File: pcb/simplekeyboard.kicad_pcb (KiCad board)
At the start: 2 copper layers, 288.1 x 97.6 mm, 164 parts, among them J1 USB_C_Receptacle_USB2.0_16P, J2 Conn_ARM_JTAG_SWD_10, SW1 SW_Push, SW10 SW_Push, SW11 SW_Push, SW12 SW_Push, SW13 SW_Push, SW14 SW_Push, SW15 SW_Push, SW16 SW_Push, SW17 SW_Push, SW18 SW_Push, SW19 SW_Push, SW2 SW_Push, SW20 SW_Push, SW21 SW_Push, SW22 SW_Push, SW23 SW_Push, SW24 SW_Push, SW25 SW_Push, SW26 SW_Push, SW27 SW_Push, SW28 SW_Push, SW29 SW_Push, SW3 SW_Push, SW30 SW_Push, SW31 SW_Push, SW32 SW_Push, SW33 SW_Push, SW34 SW_Push, SW35 SW_Push, SW36 SW_Push, SW37 SW_Push, SW38 SW_Push, SW39 SW_Push, SW4 SW_Push, SW40 SW_Push, SW41 SW_Push, SW42 SW_Push, SW43 SW_Push, SW44 SW_Push, SW45 SW_Push, SW46 SW_Push, SW47 SW_Push, SW48 SW_Push, SW49 SW_Push, SW5 SW_Push, SW50 SW_Push, SW51 SW_Push, SW52 SW_Push, SW53 SW_Push, SW54 SW_Push, SW55 SW_Push, SW56 SW_Push, SW57 SW_Push, SW58 SW_Push, SW59 SW_Push, SW6 SW_Push, SW60 SW_Push, SW61 SW_Push, SW62 SW_SPDT, SW63 SW_Push, SW7 SW_Push, SW8 SW_Push, SW9 SW_Push, U1 STM32F072CBT6, U2 USBLC6-2SC6, U3 LD39050PU33R, U4 MCP23017_SO, U5 MCP23008-xSO

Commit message: Added version marking
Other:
- board text added: "simplekeyboard v1"
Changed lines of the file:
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@@
 		(layer "Edge.Cuts")
+	)
+	(gr_text "simplekeyboard v1"
+		(at 28.575 123.825 0)
+		(layer "F.SilkS")
+		(effects
+			(font
+				(size 1.5 1.5)
+				(thickness 0.3)
+				(bold yes)
+			)
+			(justify left bottom)
+		)
 	)
 	(segment

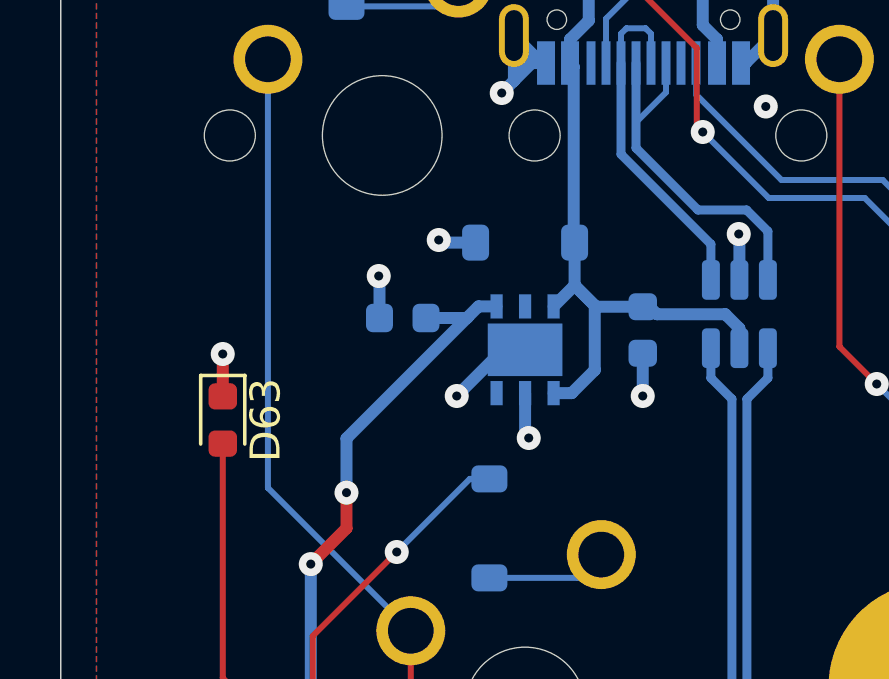
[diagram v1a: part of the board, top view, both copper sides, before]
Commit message: Added ground pad via on DFN
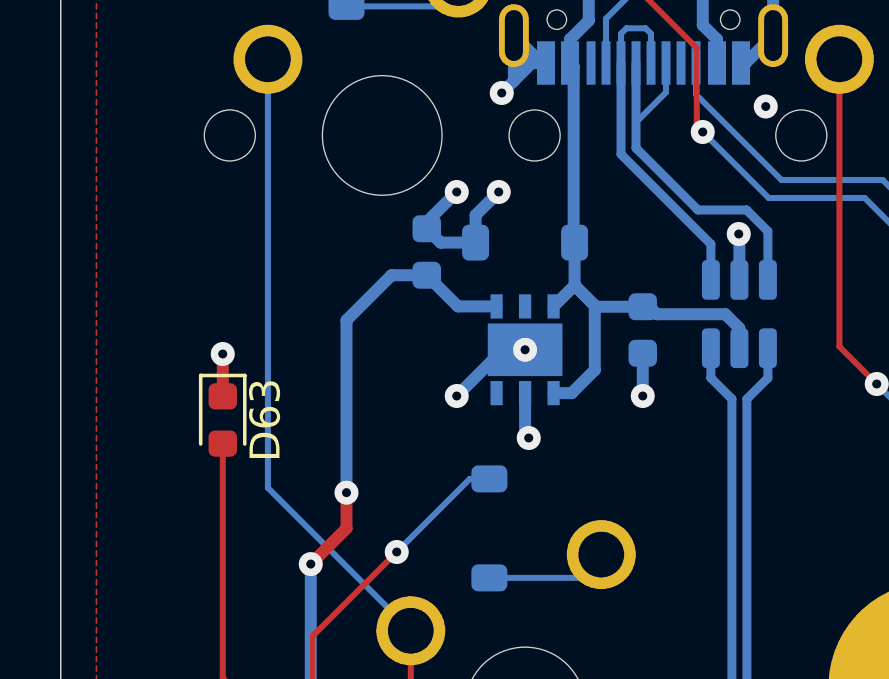
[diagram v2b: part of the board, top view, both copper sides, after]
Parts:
- moved C2 2.34 mm to (39.6, 42.0), turned to 90 degrees
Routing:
- net GND: track 63.4 -> 66.2 mm, vias 91 -> 92
- net +3.3V: track 246.7 -> 248.4 mm
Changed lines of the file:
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@@
 	(footprint "Capacitor_SMD:C_0603_1608Metric"
 		(layer "B.Cu")
-		(at 38.784375 44.184375 180)
+		(at 39.584375 41.984375 90)
 		(descr "Capacitor SMD 0603 (1608 Metric), square (rectangular) end terminal, IPC_7351 nominal, (Body size source: IPC-SM-782 page 76, https://www.pcb-3d.com/wordpress/wp-content/uploads/ipc-sm-782a_amendment_1_and_2.pdf), generated with kicad-footprint-generator")
 		(tags "capacitor")
 		(property "Reference" "C2"
-			(at -0.6 1.4 0)
+			(at -0.6 -1.484375 90)
 			(layer "B.SilkS")
 			(effects
@@
 		)
 		(property "Value" "4u7"
-			(at 0 -1.43 0)
+			(at 0 -1.43 90)
 			(layer "B.Fab")
 			(effects
@@
 		)
 		(property "Datasheet" ""
-			(at 0 0 0)
+			(at 0 0 270)
 			(unlocked yes)
 			(layer "B.Fab")
@@
 		)
 		(property "Description" "Unpolarized capacitor"
-			(at 0 0 0)
+			(at 0 0 270)
 			(unlocked yes)
 			(layer "B.Fab")
@@
 		(attr smd)
 		(fp_line
-			(start -0.14058 0.51)
-			(end 0.14058 0.51)
+			(start -0.14058 -0.51)
+			(end 0.14058 -0.51)
 			(stroke
 				(width 0.12)
@@
 		)
 		(fp_line
-			(start -0.14058 -0.51)
-			(end 0.14058 -0.51)
+			(start -0.14058 0.51)
+			(end 0.14058 0.51)
 			(stroke
 				(width 0.12)
@@
 		)
 		(fp_line
-			(start 1.48 0.73)
-			(end 1.48 -0.73)
+			(start 1.48 -0.73)
+			(end -1.48 -0.73)
 			(stroke
 				(width 0.05)
@@
 		)
 		(fp_line
-			(start 1.48 -0.73)
-			(end -1.48 -0.73)
+			(start -1.48 -0.73)
+			(end -1.48 0.73)
 			(stroke
 				(width 0.05)
@@
 		)
 		(fp_line
-			(start -1.48 0.73)
-			(end 1.48 0.73)
+			(start 1.48 0.73)
+			(end 1.48 -0.73)
 			(stroke
 				(width 0.05)
@@
 		)
 		(fp_line
-			(start -1.48 -0.73)
-			(end -1.48 0.73)
+			(start -1.48 0.73)
+			(end 1.48 0.73)
 			(stroke
 				(width 0.05)
@@
 		)
 		(fp_line
-			(start 0.8 0.4)
-			(end 0.8 -0.4)
+			(start 0.8 -0.4)
+			(end -0.8 -0.4)
 			(stroke
 				(width 0.1)
@@
 		)
 		(fp_line
-			(start 0.8 -0.4)
-			(end -0.8 -0.4)
+			(start -0.8 -0.4)
+			(end -0.8 0.4)
 			(stroke
 				(width 0.1)
@@
 		)
 		(fp_line
-			(start -0.8 0.4)
-			(end 0.8 0.4)
+			(start 0.8 0.4)
+			(end 0.8 -0.4)
 			(stroke
 				(width 0.1)
@@
 		)
 		(fp_line
-			(start -0.8 -0.4)
-			(end -0.8 0.4)
+			(start -0.8 0.4)
+			(end 0.8 0.4)
 			(stroke
 				(width 0.1)
@@
 		)
 		(fp_text user "${REFERENCE}"
-			(at 0 0 0)
+			(at 0 0 90)
 			(layer "B.Fab")
 			(effects
@@
 		)
 		(pad "1" smd roundrect
-			(at -0.775 0 180)
+			(at -0.775 0 90)
 			(size 0.9 0.95)
 			(layers "B.Cu" "B.Mask" "B.Paste")
@@
 		)
 		(pad "2" smd roundrect
-			(at 0.775 0 180)
+			(at 0.775 0 90)
 			(size 0.9 0.95)
 			(layers "B.Cu" "B.Mask" "B.Paste")
@@
 	)
 	(via
+		(at 41.984375 39.984375)
+		(size 0.8)
+		(drill 0.3)
+		(layers "F.Cu" "B.Cu")
+		(net 2)
+	)
+	(via
 		(at 48.984375 66.384375)
 		(size 0.8)
@@
 	)
 	(via
+		(at 42.8625 45.24375)
+		(size 0.8)
+		(drill 0.3)
+		(layers "F.Cu" "B.Cu")
+		(tenting none)
+		(net 2)
+	)
+	(via
 		(at 58.784375 78.184375)
 		(size 0.8)
@@
 	)
 	(via
-		(at 37.984375 42.784375)
-		(size 0.8)
-		(drill 0.3)
-		(layers "F.Cu" "B.Cu")
-		(net 2)
-	)
-	(via
 		(at 197.584375 97.384375)
 		(size 0.8)
@@
 	)
 	(via
+		(at 40.584375 39.984375)
+		(size 0.8)
+		(drill 0.3)
+		(layers "F.Cu" "B.Cu")
+		(net 2)
+	)
+	(via
 		(at 188.11875 78.58125)
 		(size 0.8)
@@
 	)
 	(via
-		(at 39.984375 41.584375)
-		(size 0.8)
-		(drill 0.3)
-		(layers "F.Cu" "B.Cu")
-		(net 2)
-	)
-	(via
 		(at 61.184375 97.784375)
 		(size 0.8)
@@
 	)
 	(segment
-		(start 38.009375 44.184375)
-		(end 38.009375 42.809375)
-		(width 0.4)
-		(layer "B.Cu")
-		(net 2)
-	)
-	(segment
 		(start 55.209375 74.409375)
 		(end 55.209375 73.009375)
@@
 	)
 	(segment
+		(start 39.584375 40.984375)
+		(end 40.584375 39.984375)
+		(width 0.4)
+		(layer "B.Cu")
+		(net 2)
+	)
+	(segment
 		(start 60.784375 75.064375)
 		(end 60.784375 76.384375)
@@
 	)
 	(segment
+		(start 41.2125 41.671875)
+		(end 41.2125 40.75625)
+		(width 0.4)
+		(layer "B.Cu")
+		(net 2)
+	)
+	(segment
 		(start 123.184375 103.104375)
 		(end 122.094325 103.104375)
@@
 	)
 	(segment
+		(start 39.584375 41.209375)
+		(end 39.584375 40.984375)
+		(width 0.4)
+		(layer "B.Cu")
+		(net 2)
+	)
+	(segment
 		(start 42.8625 48.0625)
 		(end 42.984375 48.184375)
@@
 	)
 	(segment
+		(start 40.046875 41.671875)
+		(end 39.584375 41.209375)
+		(width 0.4)
+		(layer "B.Cu")
+		(net 2)
+	)
+	(segment
 		(start 111.790625 115.378125)
 		(end 112.791875 115.378125)
@@
 	)
 	(segment
-		(start 38.009375 42.809375)
-		(end 37.984375 42.784375)
-		(width 0.4)
-		(layer "B.Cu")
-		(net 2)
-	)
-	(segment
 		(start 111.784375 115.384375)
 		(end 111.790625 115.378125)
@@
 	)
 	(segment
-		(start 41.2125 41.671875)
-		(end 40.071875 41.671875)
+		(start 51.584375 32.784375)
+		(end 51.13 33.23875)
 		(width 0.4)
 		(layer "B.Cu")
@@
 	)
 	(segment
-		(start 51.584375 32.784375)
-		(end 51.13 33.23875)
+		(start 137.31875 117.25)
+		(end 137.184375 117.384375)
 		(width 0.4)
 		(layer "B.Cu")
@@
 	)
 	(segment
-		(start 137.31875 117.25)
-		(end 137.184375 117.384375)
+		(start 41.2125 41.671875)
+		(end 40.046875 41.671875)
 		(width 0.4)
 		(layer "B.Cu")
@@
 	)
 	(segment
+		(start 41.2125 40.75625)
+		(end 41.984375 39.984375)
+		(width 0.4)
+		(layer "B.Cu")
+		(net 2)
+	)
+	(segment
 		(start 50.06 35.685)
 		(end 50.215 35.685)
@@
 	)
 	(segment
-		(start 40.071875 41.671875)
-		(end 39.984375 41.584375)
-		(width 0.4)
-		(layer "B.Cu")
-		(net 2)
-	)
-	(segment
 		(start 42.8625 45.24375)
 		(end 42.125 45.24375)
@@
 	)
 	(segment
-		(start 36.909375 48.197874)
-		(end 36.909375 50.00625)
-		(width 0.4)
-		(layer "B.Cu")
-		(net 3)
-	)
-	(segment
 		(start 58.784375 75.824376)
 		(end 60.504376 74.104375)
@@
 	)
 	(segment
+		(start 41.912499 43.79835)
+		(end 40.62335 43.79835)
+		(width 0.4)
+		(layer "B.Cu")
+		(net 3)
+	)
+	(segment
 		(start 74.2 65.64625)
 		(end 74.2 63.99625)
@@
 	)
 	(segment
-		(start 40.922873 44.184375)
-		(end 39.559375 44.184375)
-		(width 0.4)
-		(layer "B.Cu")
-		(net 3)
-	)
-	(segment
 		(start 58.184375 90.384375)
 		(end 75.984375 108.184375)
@@
 	)
 	(segment
+		(start 39.584375 42.759375)
+		(end 38.409375 42.759375)
+		(width 0.4)
+		(layer "B.Cu")
+		(net 3)
+	)
+	(segment
 		(start 49.02185 78.02185)
 		(end 49.284375 78.284375)
@@
 	)
 	(segment
-		(start 40.953624 44.153624)
-		(end 40.922873 44.184375)
+		(start 124.784375 103.959375)
+		(end 126.984375 103.959375)
 		(width 0.4)
 		(layer "B.Cu")
@@
 	)
 	(segment
-		(start 124.784375 103.959375)
-		(end 126.984375 103.959375)
+		(start 120.784375 110.384375)
+		(end 122.951875 108.216875)
 		(width 0.4)
 		(layer "B.Cu")
@@
 	)
 	(segment
-		(start 120.784375 110.384375)
-		(end 122.951875 108.216875)
+		(start 36.909375 44.259375)
+		(end 36.909375 50.00625)
 		(width 0.4)
 		(layer "B.Cu")
@@
 	)
 	(segment
+		(start 40.62335 43.79835)
+		(end 39.584375 42.759375)
+		(width 0.4)
+		(layer "B.Cu")
+		(net 3)
+	)
+	(segment
 		(start 57.864375 76.104375)
 		(end 58.784375 76.104375)
@@
 	)
 	(segment
-		(start 40.953624 44.153624)
-		(end 36.909375 48.197874)
-		(width 0.4)
-		(layer "B.Cu")
-		(net 3)
-	)
-	(segment
 		(start 126.984375 106.384375)
 		(end 132.784375 112.184375)
@@
 	)
 	(segment
-		(start 41.308899 43.79835)
-		(end 40.953624 44.153624)
+		(start 38.409375 42.759375)
+		(end 36.909375 44.259375)
 		(width 0.4)
 		(layer "B.Cu")
@@
 		(layer "B.Cu")
 		(net 3)
-	)
-	(segment
-		(start 41.912499 43.79835)
-		(end 41.308899 43.79835)
-		(width 0.4)
-		(layer "B.Cu")
-		(net 3)
